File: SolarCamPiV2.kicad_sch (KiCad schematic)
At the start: 94 parts, among them J1 TagConnect_TC2030_SWD, J2 RPi, J3 FTDI_RPI, Q1 AO3401A, Q2 AO3401A, Q3 2N7002, Q4 AO3401A, Q5 2N7002, Q6 BSS84, SW1 User, U1 CN3767, U2 HT7533, U3 SY8113B, U4 STM32G031Fx, Y1 32.768kHz

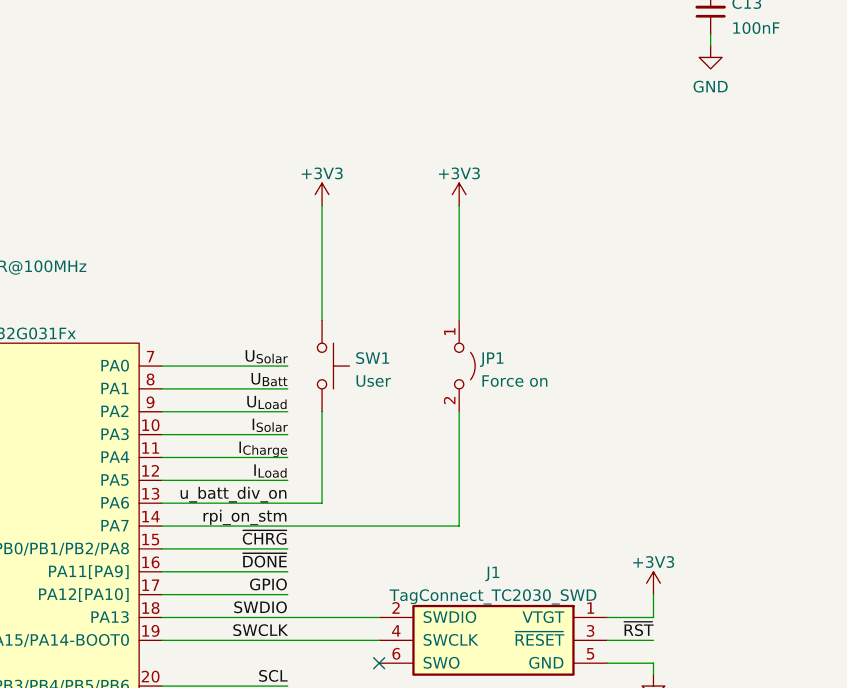
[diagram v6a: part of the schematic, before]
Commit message: Finish component placement
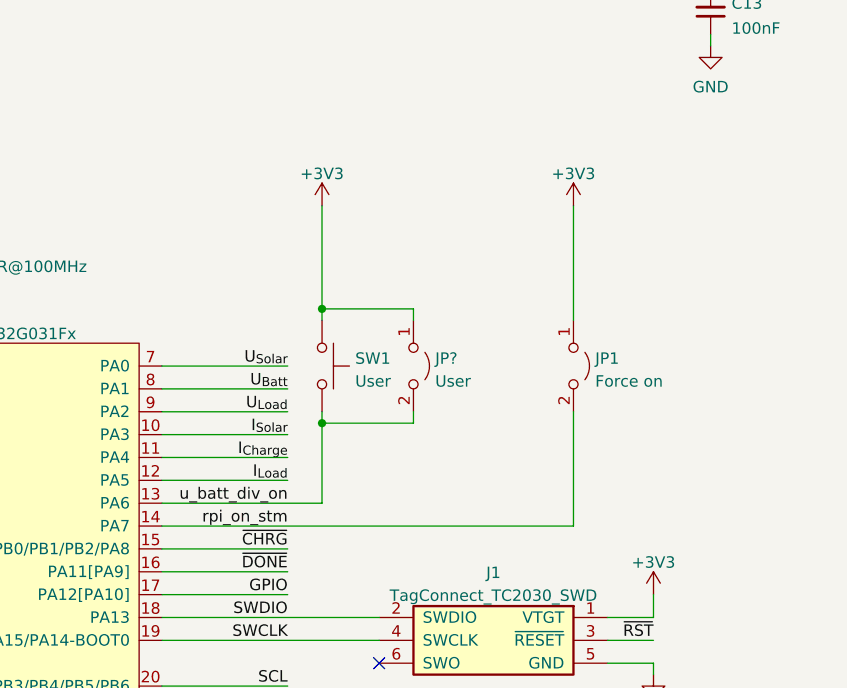
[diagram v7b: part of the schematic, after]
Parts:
- added JP?: User, Connector_PinHeader_2.54mm:PinHeader_1x02_P2.54mm_Horizontal, symbol Jumper:Jumper_2_Open
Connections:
- net +3V3: now also JP?.1 (A)
- net u_batt_div_on: now also JP?.2 (B)
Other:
- moved on the sheet: JP1
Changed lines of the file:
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@@
   (junction (at 255.27 39.37) (diameter 0) (color 0 0 0 0)
   )
+  (junction (at 130.81 154.94) (diameter 0) (color 0 0 0 0)
+  )
   (junction (at 173.99 90.17) (diameter 0) (color 0 0 0 0)
   )
@@
   (junction (at 63.5 62.23) (diameter 0) (color 0 0 0 0)
   )
+  (junction (at 130.81 142.24) (diameter 0) (color 0 0 0 0)
+  )
   (junction (at 275.59 46.99) (diameter 0) (color 0 0 0 0)
   )
@@
     (stroke (width 0) (type default) (color 0 0 0 0))
   )
-  (wire (pts (xy 146.05 130.81) (xy 146.05 143.51))
+  (wire (pts (xy 158.75 130.81) (xy 158.75 143.51))
     (stroke (width 0) (type default) (color 0 0 0 0))
   )
@@
     (stroke (width 0) (type default) (color 0 0 0 0))
   )
+  (wire (pts (xy 130.81 154.94) (xy 130.81 163.83))
+    (stroke (width 0) (type default) (color 0 0 0 0))
+  )
   (wire (pts (xy 201.93 76.2) (xy 203.2 76.2))
     (stroke (width 0) (type default) (color 0 0 0 0))
@@
     (stroke (width 0) (type default) (color 0 0 0 0))
   )
+  (wire (pts (xy 130.81 142.24) (xy 130.81 143.51))
+    (stroke (width 0) (type default) (color 0 0 0 0))
+  )
   (wire (pts (xy 62.23 90.17) (xy 66.04 90.17))
     (stroke (width 0) (type default) (color 0 0 0 0))
@@
     (stroke (width 0) (type default) (color 0 0 0 0))
   )
-  (wire (pts (xy 113.03 166.37) (xy 146.05 166.37))
-    (stroke (width 0) (type default) (color 0 0 0 0))
-  )
   (wire (pts (xy 62.23 105.41) (xy 69.85 105.41))
     (stroke (width 0) (type default) (color 0 0 0 0))
@@
     (stroke (width 0) (type default) (color 0 0 0 0))
   )
-  (wire (pts (xy 130.81 130.81) (xy 130.81 143.51))
+  (wire (pts (xy 130.81 130.81) (xy 130.81 142.24))
     (stroke (width 0) (type default) (color 0 0 0 0))
   )
@@
     (stroke (width 0) (type default) (color 0 0 0 0))
   )
+  (wire (pts (xy 113.03 166.37) (xy 158.75 166.37))
+    (stroke (width 0) (type default) (color 0 0 0 0))
+  )
   (wire (pts (xy 276.86 107.95) (xy 276.86 109.22))
     (stroke (width 0) (type default) (color 0 0 0 0))
@@
     (stroke (width 0) (type default) (color 0 0 0 0))
   )
+  (wire (pts (xy 140.97 143.51) (xy 140.97 142.24))
+    (stroke (width 0) (type default) (color 0 0 0 0))
+  )
   (wire (pts (xy 63.5 62.23) (xy 63.5 63.5))
     (stroke (width 0) (type default) (color 0 0 0 0))
@@
     (stroke (width 0) (type default) (color 0 0 0 0))
   )
+  (wire (pts (xy 140.97 142.24) (xy 130.81 142.24))
+    (stroke (width 0) (type default) (color 0 0 0 0))
+  )
   (wire (pts (xy 20.0584 138.1127) (xy 20.0584 139.3827))
     (stroke (width 0) (type default) (color 0 0 0 0))
@@
     (stroke (width 0) (type default) (color 0 0 0 0))
   )
+  (wire (pts (xy 140.97 154.94) (xy 130.81 154.94))
+    (stroke (width 0) (type default) (color 0 0 0 0))
+  )
   (wire (pts (xy 190.5 45.72) (xy 190.5 48.26))
     (stroke (width 0) (type default) (color 0 0 0 0))
@@
     (stroke (width 0) (type default) (color 0 0 0 0))
   )
-  (wire (pts (xy 146.05 153.67) (xy 146.05 166.37))
+  (wire (pts (xy 158.75 153.67) (xy 158.75 166.37))
     (stroke (width 0) (type default) (color 0 0 0 0))
   )
@@
     (stroke (width 0) (type default) (color 0 0 0 0))
   )
+  (wire (pts (xy 140.97 153.67) (xy 140.97 154.94))
+    (stroke (width 0) (type default) (color 0 0 0 0))
+  )
   (wire (pts (xy 196.85 76.2) (xy 195.58 76.2))
     (stroke (width 0) (type default) (color 0 0 0 0))
@@
     (stroke (width 0) (type default) (color 0 0 0 0))
   )
-  (wire (pts (xy 130.81 153.67) (xy 130.81 163.83))
+  (wire (pts (xy 130.81 153.67) (xy 130.81 154.94))
     (stroke (width 0) (type default) (color 0 0 0 0))
   )
@@
     (pin "2")
   )
+  (symbol (lib_id "Jumper:Jumper_2_Open") (at 140.97 148.59 270) (unit 1)
+    (in_bom yes) (on_board yes) (fields_autoplaced)
+    (property "Reference" "JP?" (id 0) (at 143.383 147.7553 90)
+      (effects (font (size 1.27 1.27)) (justify left))
+    )
+    (property "Value" "User" (id 1) (at 143.383 150.2922 90)
+      (effects (font (size 1.27 1.27)) (justify left))
+    )
+    (property "Footprint" "Connector_PinHeader_2.54mm:PinHeader_1x02_P2.54mm_Horizontal" (id 2) (at 140.97 148.59 0)
+      (effects (font (size 1.27 1.27)) hide)
+    )
+    (property "Datasheet" "~" (id 3) (at 140.97 148.59 0)
+      (effects (font (size 1.27 1.27)) hide)
+    )
+    (pin "1")
+    (pin "2")
+  )
   (symbol (lib_id "Device:FerriteBead_Small") (at 88.9 135.89 0) (unit 1)
     (in_bom yes) (on_board yes) (fields_autoplaced)
@@
     (pin "1")
   )
-  (symbol (lib_id "Jumper:Jumper_2_Open") (at 146.05 148.59 270) (unit 1)
+  (symbol (lib_id "Jumper:Jumper_2_Open") (at 158.75 148.59 270) (unit 1)
     (in_bom yes) (on_board yes) (fields_autoplaced)
-    (property "Reference" "JP1" (id 0) (at 148.463 147.7553 90)
+    (property "Reference" "JP1" (id 0) (at 161.163 147.7553 90)
       (effects (font (size 1.27 1.27)) (justify left))
     )
-    (property "Value" "Force on" (id 1) (at 148.463 150.2922 90)
+    (property "Value" "Force on" (id 1) (at 161.163 150.2922 90)
       (effects (font (size 1.27 1.27)) (justify left))
     )
-    (property "Footprint" "Connector_PinHeader_2.54mm:PinHeader_1x02_P2.54mm_Horizontal" (id 2) (at 146.05 148.59 0)
+    (property "Footprint" "Connector_PinHeader_2.54mm:PinHeader_1x02_P2.54mm_Horizontal" (id 2) (at 158.75 148.59 0)
       (effects (font (size 1.27 1.27)) hide)
     )
-    (property "Datasheet" "~" (id 3) (at 146.05 148.59 0)
+    (property "Datasheet" "~" (id 3) (at 158.75 148.59 0)
       (effects (font (size 1.27 1.27)) hide)
     )
@@
     (pin "2")
   )
-  (symbol (lib_id "power:+3V3") (at 146.05 130.81 0) (unit 1)
+  (symbol (lib_id "power:+3V3") (at 158.75 130.81 0) (unit 1)
     (in_bom yes) (on_board yes) (fields_autoplaced)
-    (property "Reference" "#PWR0147" (id 0) (at 146.05 134.62 0)
+    (property "Reference" "#PWR0147" (id 0) (at 158.75 134.62 0)
       (effects (font (size 1.27 1.27)) hide)
     )
-    (property "Value" "+3V3" (id 1) (at 146.05 127.2342 0))
-    (property "Footprint" "" (id 2) (at 146.05 130.81 0)
+    (property "Value" "+3V3" (id 1) (at 158.75 127.2342 0))
+    (property "Footprint" "" (id 2) (at 158.75 130.81 0)
       (effects (font (size 1.27 1.27)) hide)
     )
-    (property "Datasheet" "" (id 3) (at 146.05 130.81 0)
+    (property "Datasheet" "" (id 3) (at 158.75 130.81 0)
       (effects (font (size 1.27 1.27)) hide)
     )
@@
       (reference "JP3") (unit 1) (value "Pi -> PWR ON") (footprint "Jumper:SolderJumper-2_P1.3mm_Bridged_Pad1.0x1.5mm")
     )
+    (path "/80c79d4c-bd1e-491d-9024-cf67191a104a"
+      (reference "JP?") (unit 1) (value "User") (footprint "Connector_PinHeader_2.54mm:PinHeader_1x02_P2.54mm_Horizontal")
+    )
     (path "/41956ed0-8edb-4799-b456-d49581251475"
